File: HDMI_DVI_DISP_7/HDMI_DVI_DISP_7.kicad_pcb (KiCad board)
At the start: 2 copper layers, 3 parts, among them U6001 TFP401A, U6002 SN65LVDS93A

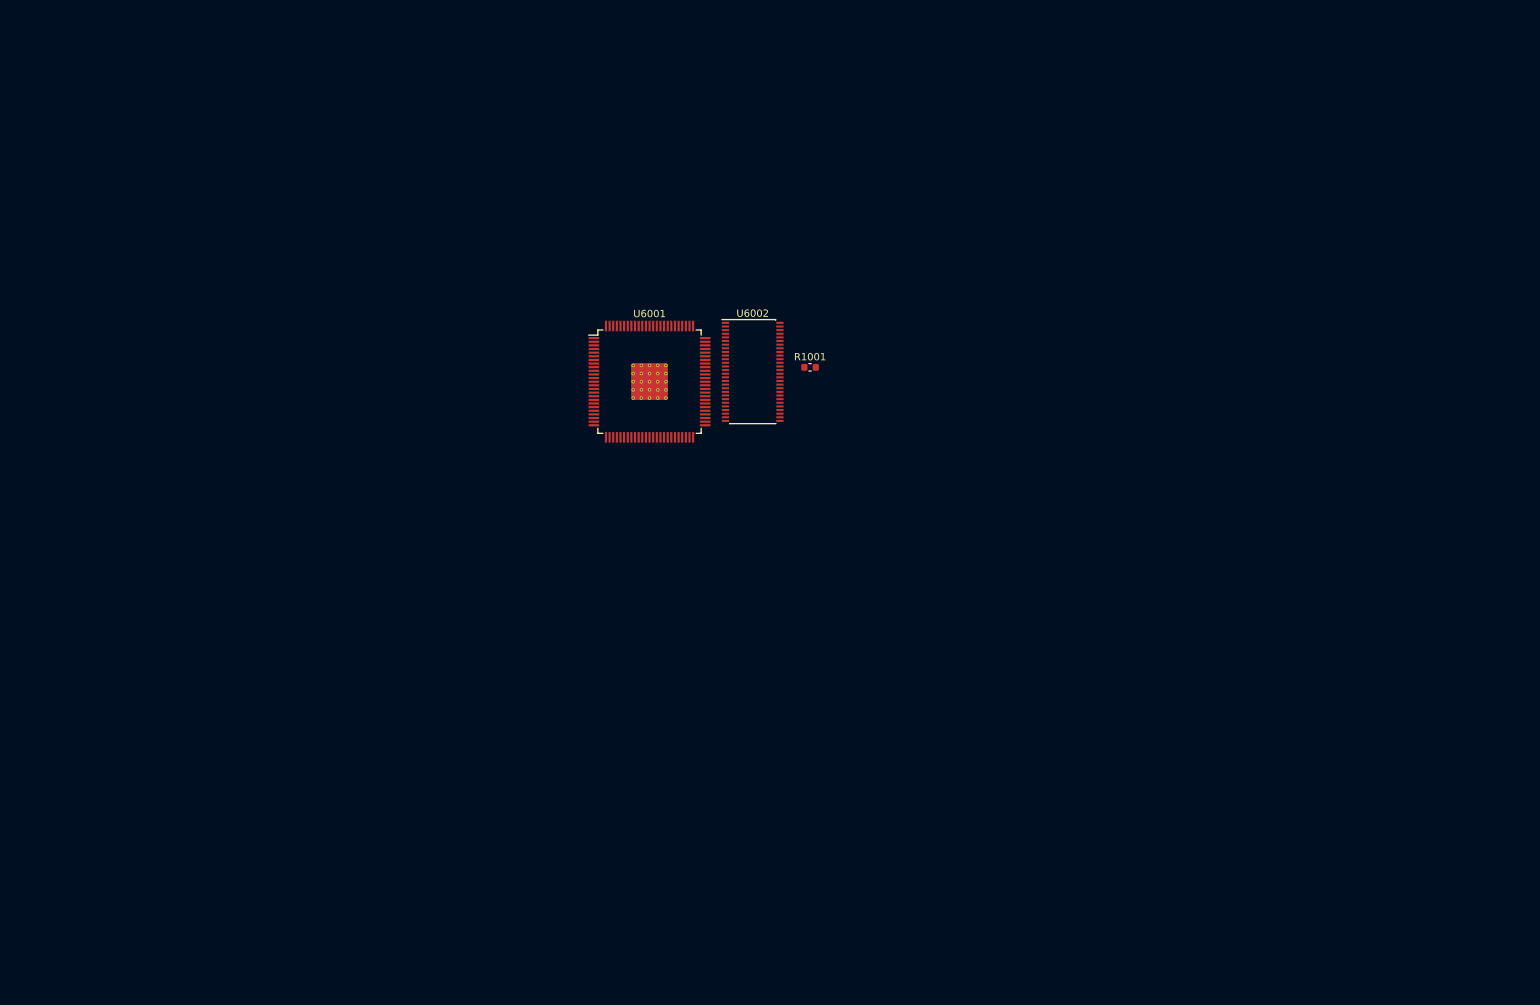
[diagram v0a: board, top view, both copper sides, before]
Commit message: All packages are added
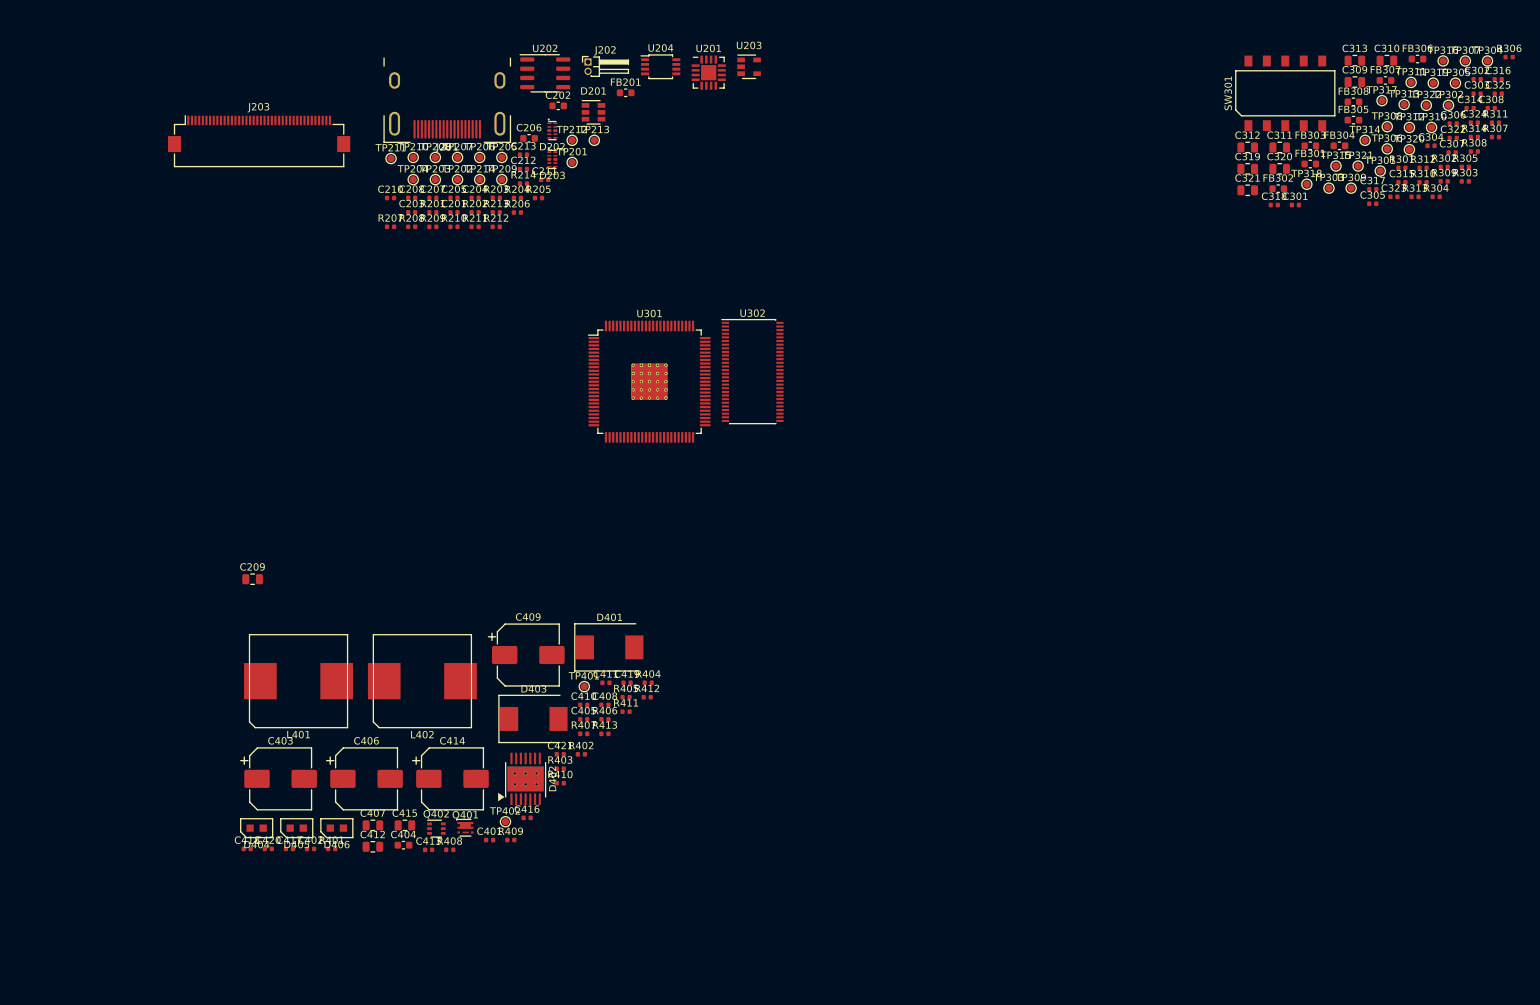
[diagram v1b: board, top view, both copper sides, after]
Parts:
- removed R1001: R, Resistor_SMD:R_0603_1608Metric
- added C201: 68n, Capacitor_SMD:C_0402_1005Metric, F.Cu at (78.0, 52.2)
- added C202: 1u, Capacitor_SMD:C_0603_1608Metric, F.Cu at (92.3, 37.6)
- added C203: 68n, Capacitor_SMD:C_0402_1005Metric, F.Cu at (72.2, 52.2)
- added C204: 68n, Capacitor_SMD:C_0402_1005Metric, F.Cu at (80.9, 50.2)
- added C205: 68n, Capacitor_SMD:C_0402_1005Metric, F.Cu at (78.0, 50.2)
- added C206: 1u, Capacitor_SMD:C_0603_1608Metric, F.Cu at (88.3, 42.0)
- added C207: 68n, Capacitor_SMD:C_0402_1005Metric, F.Cu at (75.1, 50.2)
- added C208: 10n, Capacitor_SMD:C_0402_1005Metric, F.Cu at (72.2, 50.2)
- added C209: 10u, Capacitor_SMD:C_0805_2012Metric, F.Cu at (50.3, 102.7)
- added C210: 68n, Capacitor_SMD:C_0402_1005Metric, F.Cu at (69.2, 50.3)
- added C211: 68n, Capacitor_SMD:C_0402_1005Metric, F.Cu at (90.5, 47.7)
- added C212: 1u, Capacitor_SMD:C_0402_1005Metric, F.Cu at (87.5, 46.3)
- added C213: 1u, Capacitor_SMD:C_0402_1005Metric, F.Cu at (87.5, 44.3)
- added C301: 68n, Capacitor_SMD:C_0402_1005Metric, F.Cu at (193.8, 51.2)
- added C302: 68n, Capacitor_SMD:C_0402_1005Metric, F.Cu at (218.8, 33.9)
- added C303: 68n, Capacitor_SMD:C_0402_1005Metric, F.Cu at (218.8, 35.9)
- added C304: 68n, Capacitor_SMD:C_0402_1005Metric, F.Cu at (212.5, 43.1)
- added C305: 68n, Capacitor_SMD:C_0402_1005Metric, F.Cu at (204.5, 51.0)
- added C306: 68n, Capacitor_SMD:C_0402_1005Metric, F.Cu at (215.5, 40.0)
- added C307: 68n, Capacitor_SMD:C_0402_1005Metric, F.Cu at (215.4, 44.0)
- added C308: 68n, Capacitor_SMD:C_0402_1005Metric, F.Cu at (220.8, 37.9)
- added C309: 10u, Capacitor_SMD:C_0805_2012Metric, F.Cu at (202.0, 34.3)
- added C310: 10u, Capacitor_SMD:C_0805_2012Metric, F.Cu at (206.4, 31.3)
- added C311: 10u, Capacitor_SMD:C_0805_2012Metric, F.Cu at (191.7, 43.3)
- added C312: 10u, Capacitor_SMD:C_0805_2012Metric, F.Cu at (187.2, 43.3)
- added C313: 10u, Capacitor_SMD:C_0805_2012Metric, F.Cu at (202.0, 31.3)
- added C314: 68n, Capacitor_SMD:C_0402_1005Metric, F.Cu at (217.9, 37.9)
- added C315: 68n, Capacitor_SMD:C_0402_1005Metric, F.Cu at (208.5, 48.1)
- added C316: 68n, Capacitor_SMD:C_0402_1005Metric, F.Cu at (221.7, 33.9)
- added C317: 68n, Capacitor_SMD:C_0402_1005Metric, F.Cu at (204.5, 49.1)
- added C318: 68n, Capacitor_SMD:C_0402_1005Metric, F.Cu at (190.9, 51.2)
- added C319: 10u, Capacitor_SMD:C_0805_2012Metric, F.Cu at (187.2, 46.2)
- added C320: 10u, Capacitor_SMD:C_0805_2012Metric, F.Cu at (191.7, 46.2)
- added C321: 10u, Capacitor_SMD:C_0805_2012Metric, F.Cu at (187.2, 49.2)
- added C322: 68n, Capacitor_SMD:C_0402_1005Metric, F.Cu at (215.5, 42.0)
- added C323: 68n, Capacitor_SMD:C_0402_1005Metric, F.Cu at (207.4, 50.1)
- added C324: 68n, Capacitor_SMD:C_0402_1005Metric, F.Cu at (218.4, 39.9)
- added C325: 68n, Capacitor_SMD:C_0402_1005Metric, F.Cu at (221.7, 35.9)
- added C401: 12p, Capacitor_SMD:C_0402_1005Metric, F.Cu at (82.9, 138.6)
- added C402: 10n, Capacitor_SMD:C_0402_1005Metric, F.Cu at (58.2, 139.9)
- added C403: 100u, Capacitor_SMD:CP_Elec_8x10, F.Cu at (54.1, 130.2)
- added C404: 10u, Capacitor_SMD:C_0603_1608Metric, F.Cu at (71.0, 139.3)
- added C405: 68n, Capacitor_SMD:C_0402_1005Metric, F.Cu at (95.8, 122.0)
- added C406: 100u, Capacitor_SMD:CP_Elec_8x10, F.Cu at (65.9, 130.2)
- added C407: 10u, Capacitor_SMD:C_0805_2012Metric, F.Cu at (66.8, 136.6)
- added C408: 68n, Capacitor_SMD:C_0402_1005Metric, F.Cu at (98.8, 120.0)
- added C409: 100u, Capacitor_SMD:CP_Elec_8x10, F.Cu at (88.2, 113.2)
- added C410: 68n, Capacitor_SMD:C_0402_1005Metric, F.Cu at (95.8, 120.0)
- added C411: 68n, Capacitor_SMD:C_0402_1005Metric, F.Cu at (98.9, 117.0)
- added C412: 10u, Capacitor_SMD:C_0805_2012Metric, F.Cu at (66.8, 139.6)
- added C413: 68n, Capacitor_SMD:C_0402_1005Metric, F.Cu at (74.5, 140.0)
- added C414: 100u, Capacitor_SMD:CP_Elec_8x10, F.Cu at (77.8, 130.2)
- added C415: 10u, Capacitor_SMD:C_0805_2012Metric, F.Cu at (71.2, 136.6)
- added C416: 68n, Capacitor_SMD:C_0402_1005Metric, F.Cu at (88.0, 135.6)
- added C417: 10n, Capacitor_SMD:C_0402_1005Metric, F.Cu at (55.3, 139.9)
- added C418: 12p, Capacitor_SMD:C_0402_1005Metric, F.Cu at (49.5, 139.9)
- added C419: 68n, Capacitor_SMD:C_0402_1005Metric, F.Cu at (101.8, 117.0)
- added C420: 68n, Capacitor_SMD:C_0402_1005Metric, F.Cu at (52.4, 139.9)
- added C421: 68n, Capacitor_SMD:C_0402_1005Metric, F.Cu at (92.6, 126.8)
- added D201: ESDA6V1BC6, Package_TO_SOT_SMD:SOT-23-6, F.Cu at (97.2, 38.5)
- added D202: TPD4E02B04, Yehor_lib:USON-10_-_1mm_x_2.5mm_x_0.55mm, F.Cu at (91.5, 41.0)
- added D203: TPD4E02B04, Yehor_lib:USON-10_-_1mm_x_2.5mm_x_0.55mm, F.Cu at (91.5, 44.9)
- added D401: MBRS360, Diode_SMD:D_SMC, F.Cu at (99.4, 112.1)
- added D402: TPS54286, Yehor_lib:HTSSOP-5.0x4.4-14x0.65-EP, F.Cu at (87.8, 130.2)
- added D403: MBRS360, Diode_SMD:D_SMC, F.Cu at (89.0, 122.0)
- added D404: LG V196-N1P2-24Z, Yehor_lib:OSRAM_LED_1x1x1.8, F.Cu at (50.8, 137.0)
- added D405: LG V196-N1P2-24Z, Yehor_lib:OSRAM_LED_1x1x1.8, F.Cu at (56.3, 137.0)
- added D406: LG V196-N1P2-24Z, Yehor_lib:OSRAM_LED_1x1x1.8, F.Cu at (61.9, 137.0)
- added FB201: Ferrite_Bead, Inductor_SMD:L_0603_1608Metric, F.Cu at (101.6, 35.8)
- added FB301: Ferrite_Bead, Inductor_SMD:L_0603_1608Metric, F.Cu at (195.9, 45.6)
- added FB302: Ferrite_Bead, Inductor_SMD:L_0603_1608Metric, F.Cu at (191.5, 49.0)
- added FB303: Ferrite_Bead, Inductor_SMD:L_0603_1608Metric, F.Cu at (195.9, 43.1)
- added FB304: Ferrite_Bead, Inductor_SMD:L_0603_1608Metric, F.Cu at (199.9, 43.1)
- added FB305: Ferrite_Bead, Inductor_SMD:L_0603_1608Metric, F.Cu at (201.8, 39.5)
- added FB306: Ferrite_Bead, Inductor_SMD:L_0603_1608Metric, F.Cu at (210.6, 31.1)
- added FB307: Ferrite_Bead, Inductor_SMD:L_0603_1608Metric, F.Cu at (206.2, 34.1)
- added FB308: Ferrite_Bead, Inductor_SMD:L_0603_1608Metric, F.Cu at (201.8, 37.0)
- added J201: HDMI_A, Yehor_lib:HDMI_A_19p_0.5mm, F.Cu at (77.1, 40.8)
- added J202: Jack-DC, Connector_PinHeader_1.27mm:PinHeader_1x02_P1.27mm_Horizontal, F.Cu at (96.4, 31.5)
- added J203: Conn_01x40_MountingPin, Connector_FFC-FPC:Hirose_FH12-40S-0.5SH_1x40-1MP_P0.50mm_Horizontal, F.Cu at (51.2, 41.4)
- added L401: 22u, Yehor_lib:IND_12065, F.Cu at (56.6, 116.8)
- added L402: 22u, Yehor_lib:IND_12065, F.Cu at (73.6, 116.8)
- added Q401: SiA453EDJ, Package_TO_SOT_SMD:Vishay_PowerPAK_SC70-6L_Single, F.Cu at (79.6, 136.9)
- added Q402: MUN5211DW1, Package_TO_SOT_SMD:SOT-363_SC-70-6, F.Cu at (75.6, 137.1)
- added R201: 1k, Resistor_SMD:R_0402_1005Metric, F.Cu at (75.1, 52.2)
- added R202: 1k, Resistor_SMD:R_0402_1005Metric, F.Cu at (80.9, 52.2)
- added R203: 1k, Resistor_SMD:R_0402_1005Metric, F.Cu at (83.8, 50.2)
- added R204: 1k, Resistor_SMD:R_0402_1005Metric, F.Cu at (86.7, 50.3)
- added R205: 100k, Resistor_SMD:R_0402_1005Metric, F.Cu at (89.6, 50.3)
- added R206: 4k7, Resistor_SMD:R_0402_1005Metric, F.Cu at (86.7, 52.2)
- added R207: 4k7, Resistor_SMD:R_0402_1005Metric, F.Cu at (69.2, 54.2)
- added R208: 4k7, Resistor_SMD:R_0402_1005Metric, F.Cu at (72.2, 54.2)
- added R209: 4k7, Resistor_SMD:R_0402_1005Metric, F.Cu at (75.1, 54.2)
- added R210: 1k, Resistor_SMD:R_0402_1005Metric, F.Cu at (78.0, 54.2)
- added R211: 1k, Resistor_SMD:R_0402_1005Metric, F.Cu at (80.9, 54.2)
- added R212: 4k7, Resistor_SMD:R_0402_1005Metric, F.Cu at (83.8, 54.2)
- added R213: 100k, Resistor_SMD:R_0402_1005Metric, F.Cu at (83.8, 52.2)
- added R214: 4k7, Resistor_SMD:R_0402_1005Metric, F.Cu at (87.5, 48.3)
- added R301: 1k, Resistor_SMD:R_0402_1005Metric, F.Cu at (208.5, 46.1)
- added R302: 1k, Resistor_SMD:R_0402_1005Metric, F.Cu at (214.3, 46.0)
- added R303: 1k, Resistor_SMD:R_0402_1005Metric, F.Cu at (217.2, 48.0)
- added R304: 1k, Resistor_SMD:R_0402_1005Metric, F.Cu at (213.2, 50.1)
- added R305: 50R, Resistor_SMD:R_0402_1005Metric, F.Cu at (217.2, 46.0)
- added R306: 1k, Resistor_SMD:R_0402_1005Metric, F.Cu at (223.2, 30.9)
- added R307: 1k, Resistor_SMD:R_0402_1005Metric, F.Cu at (221.4, 41.9)
- added R308: 1k, Resistor_SMD:R_0402_1005Metric, F.Cu at (218.4, 43.9)
- added R309: 1k, Resistor_SMD:R_0402_1005Metric, F.Cu at (214.3, 48.0)
- added R310: 1k, Resistor_SMD:R_0402_1005Metric, F.Cu at (211.4, 48.1)
- added R311: 1k, Resistor_SMD:R_0402_1005Metric, F.Cu at (221.4, 39.9)
- added R312: 1k, Resistor_SMD:R_0402_1005Metric, F.Cu at (211.4, 46.1)
- added R313: 1k, Resistor_SMD:R_0402_1005Metric, F.Cu at (210.3, 50.1)
- added R314: 1k, Resistor_SMD:R_0402_1005Metric, F.Cu at (218.4, 41.9)
- added R401: 13k, Resistor_SMD:R_0402_1005Metric, F.Cu at (61.1, 139.9)
- added R402: 7k5, Resistor_SMD:R_0402_1005Metric, F.Cu at (95.5, 126.8)
- added R403: 7k5, Resistor_SMD:R_0402_1005Metric, F.Cu at (92.6, 128.8)
- added R404: 7k5, Resistor_SMD:R_0402_1005Metric, F.Cu at (104.7, 117.0)
- added R405: 2k4, Resistor_SMD:R_0402_1005Metric, F.Cu at (101.7, 119.0)
- added R406: 200, Resistor_SMD:R_0402_1005Metric, F.Cu at (98.8, 122.0)
- added R407: 7k5, Resistor_SMD:R_0402_1005Metric, F.Cu at (95.8, 124.0)
- added R408: 7k5, Resistor_SMD:R_0402_1005Metric, F.Cu at (77.4, 140.0)
- added R409: 7k5, Resistor_SMD:R_0402_1005Metric, F.Cu at (85.8, 138.6)
- added R410: 7k5, Resistor_SMD:R_0402_1005Metric, F.Cu at (92.6, 130.8)
- added R411: 200, Resistor_SMD:R_0402_1005Metric, F.Cu at (101.7, 121.0)
- added R412: 2k4, Resistor_SMD:R_0402_1005Metric, F.Cu at (104.6, 119.0)
- added R413: 7k5, Resistor_SMD:R_0402_1005Metric, F.Cu at (98.8, 124.0)
- added SW301: DM-05-V, Yehor_lib:SOIC-10-DM-05, F.Cu at (192.4, 35.8)
- added TP201: TestPoint, TestPoint:TestPoint_Pad_D1.0mm, F.Cu at (94.2, 45.4)
- added TP202: TestPoint, TestPoint:TestPoint_Pad_D1.0mm, F.Cu at (78.5, 47.7)
- added TP203: TestPoint, TestPoint:TestPoint_Pad_D1.0mm, F.Cu at (75.4, 47.7)
- added TP204: TestPoint, TestPoint:TestPoint_Pad_D1.0mm, F.Cu at (72.4, 47.7)
- added TP205: TestPoint, TestPoint:TestPoint_Pad_D1.0mm, F.Cu at (84.6, 44.7)
- added TP206: TestPoint, TestPoint:TestPoint_Pad_D1.0mm, F.Cu at (81.5, 44.7)
- added TP207: TestPoint, TestPoint:TestPoint_Pad_D1.0mm, F.Cu at (78.5, 44.7)
- added TP208: TestPoint, TestPoint:TestPoint_Pad_D1.0mm, F.Cu at (75.4, 44.7)
- added TP209: TestPoint, TestPoint:TestPoint_Pad_D1.0mm, F.Cu at (84.6, 47.7)
- added TP210: TestPoint, TestPoint:TestPoint_Pad_D1.0mm, F.Cu at (72.4, 44.7)
- added TP211: TestPoint, TestPoint:TestPoint_Pad_D1.0mm, F.Cu at (69.3, 44.8)
- added TP212: TestPoint, TestPoint:TestPoint_Pad_D1.0mm, F.Cu at (94.2, 42.3)
- added TP213: TestPoint, TestPoint:TestPoint_Pad_D1.0mm, F.Cu at (97.3, 42.3)
- added TP214: TestPoint, TestPoint:TestPoint_Pad_D1.0mm, F.Cu at (81.5, 47.7)
- added TP301: TestPoint, TestPoint:TestPoint_Pad_D1.0mm, F.Cu at (205.5, 46.5)
- added TP302: TestPoint, TestPoint:TestPoint_Pad_D1.0mm, F.Cu at (214.9, 37.5)
- added TP303: TestPoint, TestPoint:TestPoint_Pad_D1.0mm, F.Cu at (198.4, 48.9)
- added TP304: TestPoint, TestPoint:TestPoint_Pad_D1.0mm, F.Cu at (220.3, 31.4)
- added TP305: TestPoint, TestPoint:TestPoint_Pad_D1.0mm, F.Cu at (215.8, 34.4)
- added TP306: TestPoint, TestPoint:TestPoint_Pad_D1.0mm, F.Cu at (206.5, 43.5)
- added TP307: TestPoint, TestPoint:TestPoint_Pad_D1.0mm, F.Cu at (217.2, 31.4)
- added TP308: TestPoint, TestPoint:TestPoint_Pad_D1.0mm, F.Cu at (206.5, 40.4)
- added TP309: TestPoint, TestPoint:TestPoint_Pad_D1.0mm, F.Cu at (201.5, 48.9)
- added TP310: TestPoint, TestPoint:TestPoint_Pad_D1.0mm, F.Cu at (212.6, 40.5)
- added TP311: TestPoint, TestPoint:TestPoint_Pad_D1.0mm, F.Cu at (209.7, 34.3)
- added TP312: TestPoint, TestPoint:TestPoint_Pad_D1.0mm, F.Cu at (209.5, 40.5)
- added TP313: TestPoint, TestPoint:TestPoint_Pad_D1.0mm, F.Cu at (208.8, 37.4)
- added TP314: TestPoint, TestPoint:TestPoint_Pad_D1.0mm, F.Cu at (203.4, 42.3)
- added TP315: TestPoint, TestPoint:TestPoint_Pad_D1.0mm, F.Cu at (199.4, 45.8)
- added TP316: TestPoint, TestPoint:TestPoint_Pad_D1.0mm, F.Cu at (214.2, 31.4)
- added TP317: TestPoint, TestPoint:TestPoint_Pad_D1.0mm, F.Cu at (205.7, 36.8)
- added TP318: TestPoint, TestPoint:TestPoint_Pad_D1.0mm, F.Cu at (195.4, 48.4)
- added TP319: TestPoint, TestPoint:TestPoint_Pad_D1.0mm, F.Cu at (212.8, 34.4)
- added TP320: TestPoint, TestPoint:TestPoint_Pad_D1.0mm, F.Cu at (209.5, 43.6)
- added TP321: TestPoint, TestPoint:TestPoint_Pad_D1.0mm, F.Cu at (202.4, 45.8)
- added TP322: TestPoint, TestPoint:TestPoint_Pad_D1.0mm, F.Cu at (211.8, 37.5)
- added TP401: TestPoint, TestPoint:TestPoint_Pad_D1.0mm, F.Cu at (95.9, 117.5)
- added TP402: TestPoint, TestPoint:TestPoint_Pad_D1.0mm, F.Cu at (85.1, 136.1)
- added U201: ADG633YCP, Package_CSP:LFCSP-16-1EP_4x4mm_P0.65mm_EP2.1x2.1mm, F.Cu at (113.0, 33.0)
- added U202: 24LC32, Package_SO:SOIC-8_3.9x4.9mm_P1.27mm, F.Cu at (90.5, 33.1)
- added U203: LP2985-3.3, Package_TO_SOT_SMD:SOT-23-5, F.Cu at (118.6, 32.2)
- added U204: TXB0102DCT, Package_SO:TSSOP-8_3x3mm_P0.65mm, F.Cu at (106.4, 32.2)
- renumbered U6001 to U301, U6002 to U302
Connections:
- U301 pad 1: (no net) -> /900_Video_Links/ODF
- U301 pad 100: (no net) -> /900_Video_Links/TMDS_OCK
- U301 pad 101: Net-(U6001-Pad101) -> GNDD
- U301 pad 18: (no net) -> /900_Video_Links/P_TMDS_OVDD_3V3
- U301 pad 19: (no net) -> GNDD
- U301 pad 2: (no net) -> /900_Video_Links/~PD
- U301 pad 28: (no net) -> /900_Video_Links/P_TMDS_OVDD_3V3
- U301 pad 29: (no net) -> GNDD
- U301 pad 3: (no net) -> /900_Video_Links/DST
- U301 pad 38: (no net) -> /900_Video_Links/P_TMDS_OVDD_3V3
- U301 pad 39: (no net) -> GNDD
- U301 pad 4: (no net) -> /900_Video_Links/DI_2PPC_EN
- U301 pad 40: (no net) -> /900_Video_Links/CTL1
- U301 pad 41: (no net) -> /900_Video_Links/CTL2
- U301 pad 42: (no net) -> /900_Video_Links/CTL3
- U301 pad 43: (no net) -> /900_Video_Links/P_TMDS_OVDD_3V3
- U301 pad 45: (no net) -> GNDD
- U301 pad 5: (no net) -> GNDD
- U301 pad 57: (no net) -> /900_Video_Links/P_TMDS_OVDD_3V3
- U301 pad 58: (no net) -> GNDD
- U301 pad 6: (no net) -> /900_Video_Links/P_TMDS_DVDD_3V3
- U301 pad 67: (no net) -> /900_Video_Links/P_TMDS_DVDD_3V3
- U301 pad 68: (no net) -> GNDD
- U301 pad 7: (no net) -> /900_Video_Links/~DI_STAG_EN
- U301 pad 76: (no net) -> GNDD
- U301 pad 78: (no net) -> /900_Video_Links/P_TMDS_OVDD_3V3
- U301 pad 79: (no net) -> GNDD
- U301 pad 8: (no net) -> /DO_SYNC_DET
- U301 pad 80: (no net) -> /100_Conenctors/DI_TMDS_7
- U301 pad 81: (no net) -> /100_Conenctors/DI_TMDS_6
- U301 pad 82: (no net) -> /900_Video_Links/P_TMDS_AVDD_3V3
- U301 pad 83: (no net) -> GNDD
- U301 pad 84: (no net) -> /900_Video_Links/P_TMDS_AVDD_3V3
- U301 pad 85: (no net) -> /100_Conenctors/DI_TMDS_5
- U301 pad 86: (no net) -> /100_Conenctors/DI_TMDS_4
- U301 pad 87: (no net) -> GNDD
- U301 pad 88: (no net) -> /900_Video_Links/P_TMDS_AVDD_3V3
- U301 pad 89: (no net) -> GNDD
- U301 pad 9: (no net) -> /900_Video_Links/~PDO
- U301 pad 90: (no net) -> /100_Conenctors/DI_TMDS_3
- U301 pad 91: (no net) -> /100_Conenctors/DI_TMDS_2
- U301 pad 92: (no net) -> GNDD
- U301 pad 93: (no net) -> /100_Conenctors/DI_TMDS_1
- U301 pad 94: (no net) -> /100_Conenctors/DI_TMDS_0
- U301 pad 95: (no net) -> /900_Video_Links/P_TMDS_AVDD_3V3
- U301 pad 96: (no net) -> /900_Video_Links/AI_EXT_50R_TERM
- U301 pad 97: (no net) -> /900_Video_Links/P_TMDS_PLL_3V3
- U301 pad 98: (no net) -> GNDD
- U301 pad 99: (no net) -> /900_Video_Links/AI_RSVD_LOW
- U302 pad 1: (no net) -> /900_Video_Links/P_LVDS_IOVCC_3V3
- U302 pad 13: (no net) -> GNDD
- U302 pad 17: (no net) -> /900_Video_Links/LVDS_OCK
- U302 pad 21: (no net) -> GNDD
- U302 pad 26: (no net) -> /900_Video_Links/P_LVDS_IOVCC_3V3
- U302 pad 29: (no net) -> GNDD
- U302 pad 32: (no net) -> /900_Video_Links/LVDS_EN
- U302 pad 33: (no net) -> GNDD
- U302 pad 34: (no net) -> /900_Video_Links/P_LVDS_PLL_3V3
- U302 pad 35: (no net) -> GNDD
- U302 pad 36: (no net) -> GNDD
- U302 pad 39: (no net) -> /100_Conenctors/DO_LVDS_9
- U302 pad 40: (no net) -> /100_Conenctors/DO_LVDS_8
- U302 pad 41: (no net) -> /100_Conenctors/DO_LVDS_5
- U302 pad 42: (no net) -> /100_Conenctors/DO_LVDS_4
- U302 pad 43: (no net) -> GNDD
- U302 pad 44: (no net) -> /900_Video_Links/P_LVDSVCC_3V3
- U302 pad 45: (no net) -> /100_Conenctors/DO_LVDS_3
- U302 pad 46: (no net) -> /100_Conenctors/DO_LVDS_2
- U302 pad 47: (no net) -> /100_Conenctors/DO_LVDS_1
- U302 pad 48: /DO_LVDS_0 -> /100_Conenctors/DO_LVDS_0
- U302 pad 49: (no net) -> GNDD
- U302 pad 5: (no net) -> GNDD
- U302 pad 53: (no net) -> GNDD
- U302 pad 9: (no net) -> /900_Video_Links/P_LVDS_VCC_3V3

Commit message: Packages are done. Only few are missing. Layout started
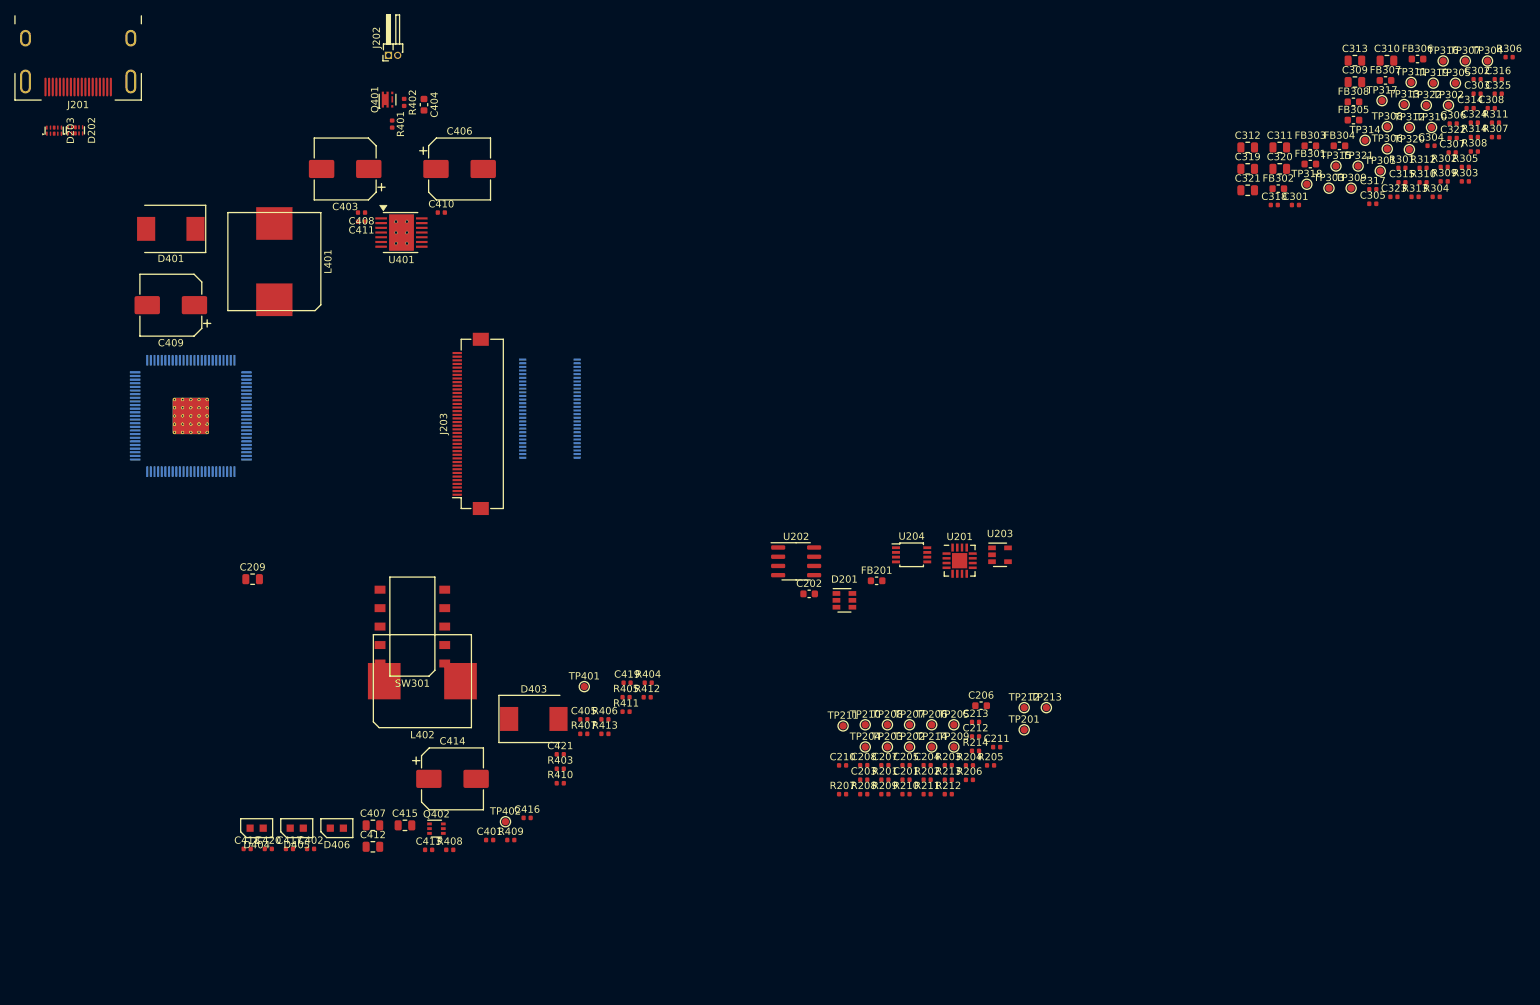
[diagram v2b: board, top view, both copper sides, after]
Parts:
- U301, U302: moved to B.Cu
- moved SW301 140.8 mm to (72.2, 109.2), turned to 90 degrees
- moved C404 102.0 mm to (73.9, 37.4), turned to 270 degrees
- moved Q401 100.8 mm to (68.8, 36.7), turned to 90 degrees
- moved R401 100.1 mm to (69.5, 40.1), turned to 270 degrees
- moved C201 99.9 mm to (140.2, 130.3)
- moved C203 99.9 mm to (134.4, 130.3)
- moved C210 99.9 mm to (131.5, 128.4)
- moved R201 99.9 mm to (137.3, 130.3)
- moved R205 99.9 mm to (151.8, 128.4)
- moved TP204 99.9 mm to (134.6, 125.8)
- moved C204 99.9 mm to (143.1, 128.3)
- moved C205 99.9 mm to (140.2, 128.3)
- moved C206 99.9 mm to (150.5, 120.1)
- moved C207 99.9 mm to (137.3, 128.3)
- moved C208 99.9 mm to (134.4, 128.3)
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- renumbered D402 to U401

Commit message: PS Layout done
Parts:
- removed C317: 68n, Capacitor_SMD:C_0402_1005Metric
- C315, C316, C318: moved to B.Cu
- moved C316 159.8 mm to (69.4, 82.2), turned to 90 degrees
- moved C315 147.3 mm to (65.2, 82.2), turned to 90 degrees
- moved C313 135.2 mm to (74.0, 74.8), turned to 90 degrees
- moved FB305 132.6 mm to (74.8, 77.6)
- moved C318 132.0 mm to (62.6, 82.2), turned to 90 degrees
- moved C420 104.1 mm to (138.6, 81.5)
- moved J203 104.0 mm to (182.0, 102.8)
- moved D405 97.2 mm to (137.6, 83.7), turned to 180 degrees
- moved C415 87.1 mm to (137.1, 79.7)
- moved D406 86.8 mm to (112.0, 66.2), turned to 90 degrees
- moved C414 79.6 mm to (132.0, 72.0), turned to 90 degrees
- moved C418 78.8 mm to (109.8, 89.1), turned to 180 degrees
- moved R409 76.3 mm to (136.4, 81.5)
- moved C417 76.1 mm to (109.8, 86.7)
- moved C412 71.9 mm to (111.2, 83.0), turned to 270 degrees
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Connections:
- net /100_Conenctors/DI_TMDS_0 renamed /100_Conenctors/DI_TMDS_CLK-
- net /100_Conenctors/DI_TMDS_1 renamed /100_Conenctors/DI_TMDS_CLK+
- net /100_Conenctors/DI_TMDS_2 renamed /100_Conenctors/DI_TMDS_D0-
- net /100_Conenctors/DI_TMDS_3 renamed /100_Conenctors/DI_TMDS_D0+
- net /100_Conenctors/DI_TMDS_4 renamed /100_Conenctors/DI_TMDS_D1-
- net /100_Conenctors/DI_TMDS_5 renamed /100_Conenctors/DI_TMDS_D1+
- net /100_Conenctors/DI_TMDS_6 renamed /100_Conenctors/DI_TMDS_D2-
- net /100_Conenctors/DI_TMDS_7 renamed /100_Conenctors/DI_TMDS_D2+
- net /100_Conenctors/DO_LVDS_0 renamed /100_Conenctors/DO_LVDS_D0-
- net /100_Conenctors/DO_LVDS_1 renamed /100_Conenctors/DO_LVDS_D0+
- net /100_Conenctors/DO_LVDS_2 renamed /100_Conenctors/DO_LVDS_D1-
- net /100_Conenctors/DO_LVDS_3 renamed /100_Conenctors/DO_LVDS_D1+
- net /100_Conenctors/DO_LVDS_4 renamed /100_Conenctors/DO_LVDS_D2-
- net /100_Conenctors/DO_LVDS_5 renamed /100_Conenctors/DO_LVDS_D2+
- net /100_Conenctors/DO_LVDS_8 renamed /100_Conenctors/DO_LVDS_CLK-
- net /100_Conenctors/DO_LVDS_9 renamed /100_Conenctors/DO_LVDS_CLK+
- C420 pad 1: (no net) -> Net-(C420-Pad1)
- C421 pad 1: (no net) -> Net-(C421-Pad1)
- D405 pad 2: Net-(D405-Pad2) -> Net-(C420-Pad1)
- D406 pad 2: Net-(D406-Pad2) -> Net-(C421-Pad1)
- R409 pad 2: Net-(D405-Pad2) -> Net-(C420-Pad1)
- R410 pad 2: Net-(D406-Pad2) -> Net-(C421-Pad1)
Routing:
- net /100_Conenctors/DI_TMDS_D1+: track 0.00 -> 23.7 mm, vias 0 -> 1
- net /100_Conenctors/DI_TMDS_D1-: track 0.00 -> 23.6 mm, vias 0 -> 1
- net /100_Conenctors/DI_TMDS_D2-: track 0.00 -> 23.5 mm, vias 0 -> 1
- net /100_Conenctors/DI_TMDS_CLK+: track 0.00 -> 23.5 mm, vias 0 -> 1
- net /100_Conenctors/DI_TMDS_D0+: track 0.00 -> 23.5 mm, vias 0 -> 1
- net /100_Conenctors/DI_TMDS_D2+: track 0.00 -> 23.3 mm, vias 0 -> 1
- net /100_Conenctors/DI_TMDS_D0-: track 0.00 -> 23.3 mm, vias 0 -> 1
- net /100_Conenctors/DI_TMDS_CLK-: track 0.00 -> 23.3 mm, vias 0 -> 1
- net /600_Power_Units/~EN_3V3: track 0.00 -> 21.0 mm, vias 0 -> 2
- net /600_Power_Units/~EN_5V: track 0.00 -> 20.8 mm, vias 0 -> 2
- net /600_Power_Units/BP_5V: track 0.00 -> 12.8 mm, vias 0 -> 2
- net /900_Video_Links/P_TMDS_AVDD_3V3: track 0.00 -> 11.0 mm, vias 0 -> 6
- net Net-(C401-Pad2): track 0.00 -> 7.11 mm
- net Net-(C417-Pad1): track 0.00 -> 7.07 mm
- net GNDD: track 0.00 -> 6.57 mm
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- added copper zone on F.Cu, net /600_Power_Units/P_VIN_FILTERED
- added copper zone on F.Cu, net /900_Video_Links/P_TMDS_AVDD_3V3
- added copper zone on F.Cu, net /P_SMPS_3V3
- added copper zone on F.Cu, net /P_SMPS_5V
- added copper zone on F.Cu, net Net-(C411-Pad2)
- added copper zone on F.Cu, net Net-(C413-Pad2)
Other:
- copper layers 2 -> 4
- net class D100 added: clearance 0.15, trace_width 0.25, via_dia 0.65, via_drill 0.25
- net class Default: clearance 0.2 -> 0.15; via_dia 0.8 -> 0.65; via_drill 0.4 -> 0.25
- net class GND added: clearance 0.15, trace_width 0.2, via_dia 0.4, via_drill 0.25
- net class Power added: clearance 0.15, trace_width 0.35, via_dia 0.65, via_drill 0.25
- net class S50 added: clearance 0.15, trace_width 0.25, via_dia 0.4, via_drill 0.25
- rule trace_clearance: 0.2 -> 0.15
- rule via_min_drill: 0.3 -> 0.15
- rule via_min_size: 0.4 -> 0.2
